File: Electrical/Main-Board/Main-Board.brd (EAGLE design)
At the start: 160 x 100 mm, 0 parts

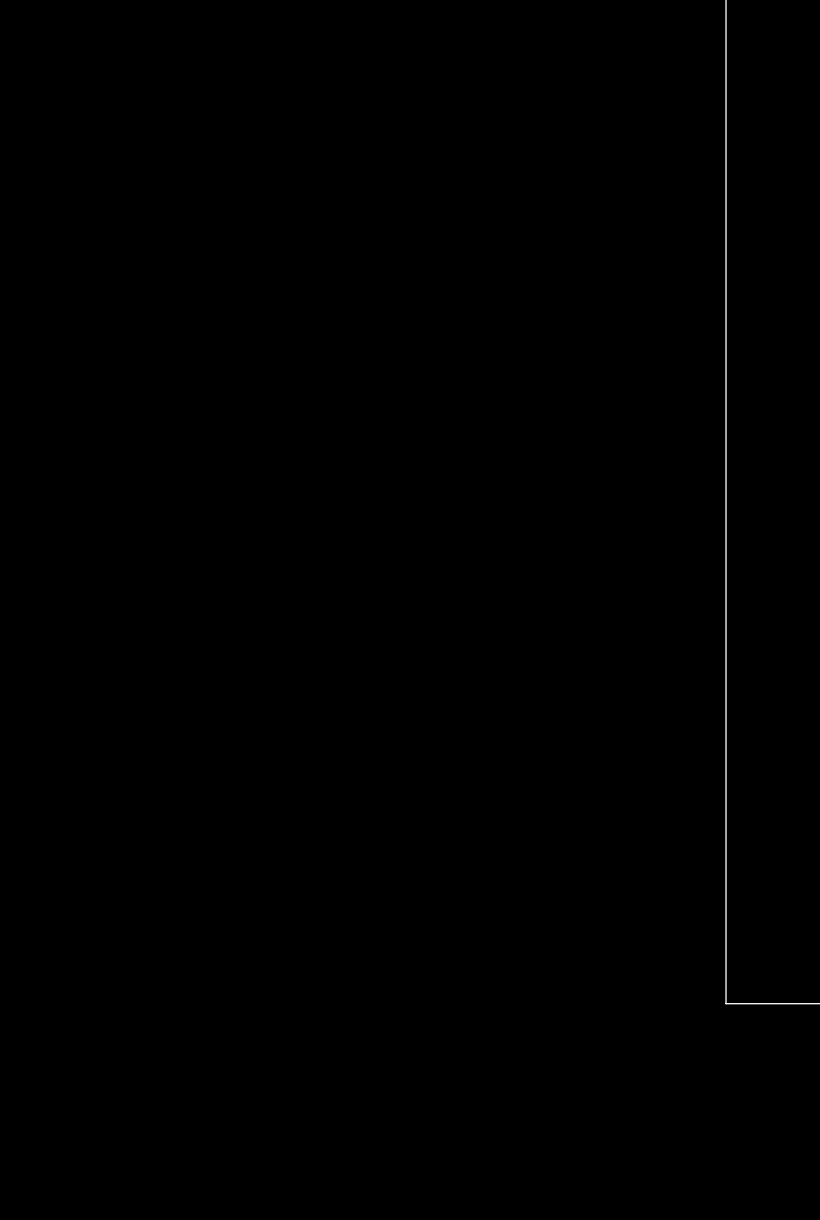
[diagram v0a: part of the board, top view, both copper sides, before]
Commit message: Updated schematic and ignore all backup files
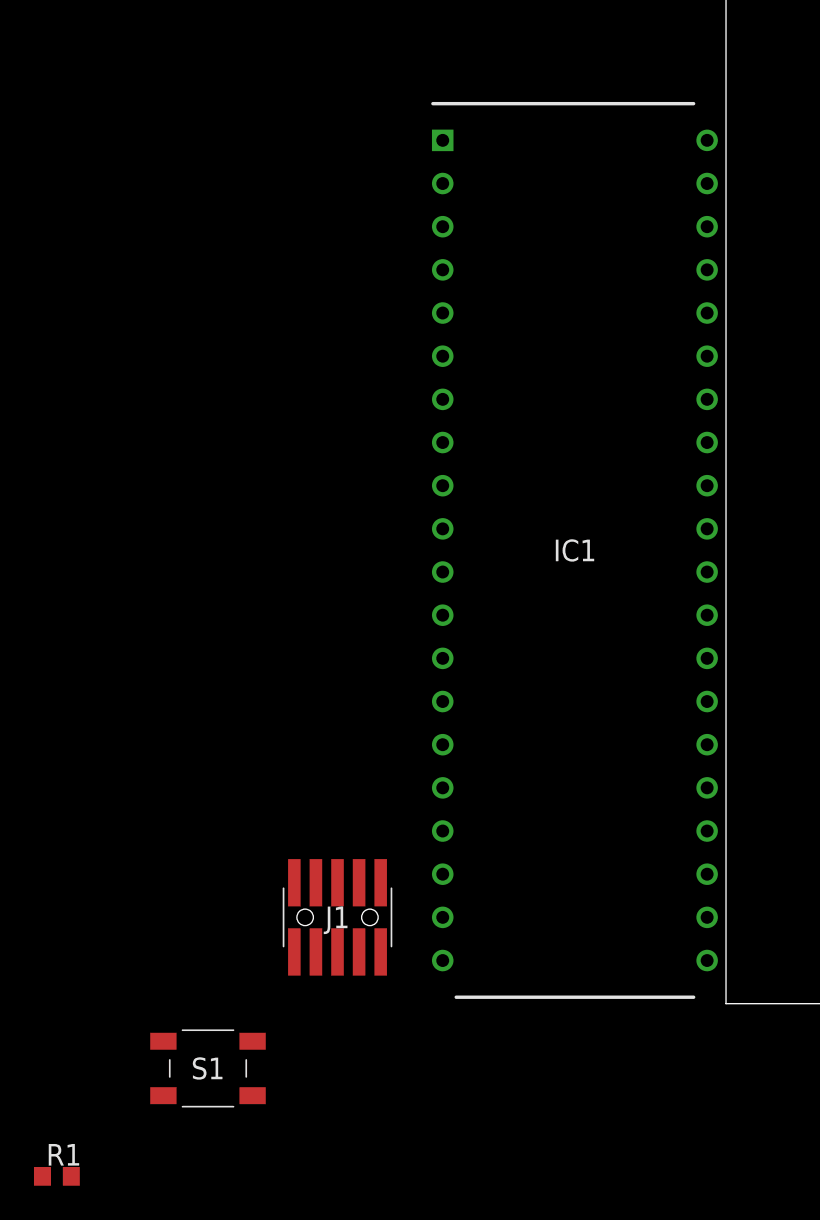
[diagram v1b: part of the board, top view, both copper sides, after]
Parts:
- added IC1: ATMEGA16A-PU, SamacSys_Parts:DIP1556W56P254L5232H483Q40N
- added J1: FTSH-105-01-L-DV-K-A-P-TR, SamacSys_Parts:FTSH10501LDVKAPTR
- added R1: 10K/10%, rcl:R0603
- added S1: PTS647SM50SMTR2LFS, SamacSys_Parts:PTS647SM50SMTR2LFS
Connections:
- new net +5V/1: IC1.10, IC1.30, IC1.32, J1.7, R1.2
- new net GND: IC1.11, IC1.31, J1.10, J1.6, S1.3, S1.4
- new net RST: IC1.9, J1.8, R1.1, S1.1, S1.2
- new net TCK: IC1.24, J1.1
- new net TDI: IC1.27, J1.5
- new net TDO: IC1.26, J1.2
- new net TMS: IC1.25, J1.3
- new net TRST: J1.9
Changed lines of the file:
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@@
 <drawing>
 <settings>
-<setting alwaysvectorfont="yes"/>
+<setting alwaysvectorfont="no"/>
 <setting verticaltext="up"/>
 </settings>
@@
 </autorouter>
 <elements>
+<element name="IC1" library="SamacSys_Parts" package="DIP1556W56P254L5232H483Q40N" value="ATMEGA16A-PU" x="-8.89" y="26.67" smashed="yes">
+<attribute name="DESCRIPTION" value="ATMEGA16A-PU, 8 bit AVR Microcontroller 16MHz 16 kB, 512 B Flash, 1 kB RAM, I2C 40-Pin PDIP" x="-8.89" y="26.67" size="1.778" layer="27" display="off"/>
+<attribute name="HEIGHT" value="4.826mm" x="-8.89" y="26.67" size="1.778" layer="27" display="off"/>
+<attribute name="MANUFACTURER_NAME" value="Microchip" x="-8.89" y="26.67" size="1.778" layer="27" display="off"/>
+<attribute name="MANUFACTURER_PART_NUMBER" value="ATMEGA16A-PU" x="-8.89" y="26.67" size="1.778" layer="27" display="off"/>
+<attribute name="MOUSER_PART_NUMBER" value="556-ATMEGA16A-PU" x="-8.89" y="26.67" size="1.778" layer="27" display="off"/>
+<attribute name="MOUSER_PRICE-STOCK" value="https://www.mouser.com/Search/Refine.aspx?Keyword=556-ATMEGA16A-PU" x="-8.89" y="26.67" size="1.778" layer="27" display="off"/>
+<attribute name="NAME" x="-8.89" y="26.67" size="1.27" layer="25" align="center"/>
+<attribute name="RS_PART_NUMBER" value="6962421P" x="-8.89" y="26.67" size="1.778" layer="27" display="off"/>
+<attribute name="RS_PRICE-STOCK" value="http://uk.rs-online.com/web/p/products/6962421P" x="-8.89" y="26.67" size="1.778" layer="27" display="off"/>
+<attribute name="VALUE" x="-8.89" y="26.67" size="1.27" layer="27" align="center"/>
+</element>
+<element name="J1" library="SamacSys_Parts" package="FTSH10501LDVKAPTR" value="FTSH-105-01-L-DV-K-A-P-TR" x="-22.86" y="5.08" smashed="yes">
+<attribute name="DESCRIPTION" value="Samtec FTSH, 1.27mm Pitch, 10 Way, 2 Row PCB Terminal Block Header, Surface Mount, Through Hole" x="-22.86" y="5.08" size="1.778" layer="27" display="off"/>
+<attribute name="HEIGHT" value="6.1mm" x="-22.86" y="5.08" size="1.778" layer="27" display="off"/>
+<attribute name="MANUFACTURER_NAME" value="SAMTEC" x="-22.86" y="5.08" size="1.778" layer="27" display="off"/>
+<attribute name="MANUFACTURER_PART_NUMBER" value="FTSH-105-01-L-DV-K-A-P-TR" x="-22.86" y="5.08" size="1.778" layer="27" display="off"/>
+<attribute name="MOUSER_PART_NUMBER" value="200-FTSH1051LDVKAPTR" x="-22.86" y="5.08" size="1.778" layer="27" display="off"/>
+<attribute name="MOUSER_PRICE-STOCK" value="https://www.mouser.com/Search/Refine.aspx?Keyword=200-FTSH1051LDVKAPTR" x="-22.86" y="5.08" size="1.778" layer="27" display="off"/>
+<attribute name="NAME" x="-22.86" y="5.08" size="1.27" layer="25" align="center"/>
+<attribute name="RS_PART_NUMBER" value="1802978P" x="-22.86" y="5.08" size="1.778" layer="27" display="off"/>
+<attribute name="RS_PRICE-STOCK" value="http://uk.rs-online.com/web/p/products/1802978P" x="-22.86" y="5.08" size="1.778" layer="27" display="off"/>
+<attribute name="VALUE" x="-22.86" y="5.08" size="1.27" layer="27" align="center"/>
+</element>
+<element name="S1" library="SamacSys_Parts" package="PTS647SM50SMTR2LFS" value="PTS647SM50SMTR2LFS" x="-30.48" y="-3.81" smashed="yes">
+<attribute name="DESCRIPTION" value="Tactile Switches 50mA 12VDC, 1.8N 5.0mm H, G leads" x="-30.48" y="-3.81" size="1.778" layer="27" display="off"/>
+<attribute name="HEIGHT" value="5.25mm" x="-30.48" y="-3.81" size="1.778" layer="27" display="off"/>
+<attribute name="MANUFACTURER_NAME" value="C &amp; K COMPONENTS" x="-30.48" y="-3.81" size="1.778" layer="27" display="off"/>
+<attribute name="MANUFACTURER_PART_NUMBER" value="PTS647SM50SMTR2LFS" x="-30.48" y="-3.81" size="1.778" layer="27" display="off"/>
+<attribute name="MOUSER_PART_NUMBER" value="611-PTS647SM50SMTR2L" x="-30.48" y="-3.81" size="1.778" layer="27" display="off"/>
+<attribute name="MOUSER_PRICE-STOCK" value="https://www.mouser.com/Search/Refine.aspx?Keyword=611-PTS647SM50SMTR2L" x="-30.48" y="-3.81" size="1.778" layer="27" display="off"/>
+<attribute name="NAME" x="-30.48" y="-3.81" size="1.27" layer="25" align="center"/>
+<attribute name="RS_PART_NUMBER" value="" x="-30.48" y="-3.81" size="1.778" layer="27" display="off"/>
+<attribute name="RS_PRICE-STOCK" value="" x="-30.48" y="-3.81" size="1.778" layer="27" display="off"/>
+<attribute name="VALUE" x="-30.48" y="-3.81" size="1.27" layer="27" align="center"/>
+</element>
+<element name="R1" library="rcl" library_urn="urn:adsk.eagle:library:334" package="R0603" package3d_urn="urn:adsk.eagle:package:23555/3" value="10K/10%" x="-39.37" y="-10.16" smashed="yes">
+<attribute name="NAME" x="-40.005" y="-9.525" size="1.27" layer="25"/>
+<attribute name="POPULARITY" value="70" x="-39.37" y="-10.16" size="1.778" layer="27" display="off"/>
+<attribute name="SPICEPREFIX" value="R" x="-39.37" y="-10.16" size="1.778" layer="27" display="off"/>
+<attribute name="VALUE" x="-40.005" y="-12.065" size="1.27" layer="27"/>
+</element>
 </elements>
 <signals>
+<signal name="GND">
+<contactref element="IC1" pad="11"/>
+<contactref element="IC1" pad="31"/>
+<contactref element="J1" pad="6"/>
+<contactref element="J1" pad="10"/>
+<contactref element="S1" pad="4"/>
+<contactref element="S1" pad="3"/>
+<wire x1="-27.855" y1="-2.21" x2="-27.855" y2="-5.41" width="0" layer="19" extent="1-1"/>
+<wire x1="-22.86" y1="7.115" x2="-27.855" y2="-2.21" width="0" layer="19" extent="1-1"/>
+<wire x1="-20.32" y1="7.115" x2="-22.86" y2="7.115" width="0" layer="19" extent="1-1"/>
+<wire x1="-16.669" y1="25.4" x2="-20.32" y2="7.115" width="0" layer="19" extent="1-1"/>
+<wire x1="-1.111" y1="27.94" x2="-16.669" y2="25.4" width="0" layer="19" extent="1-1"/>
+</signal>
+<signal name="+5V/1">
+<contactref element="IC1" pad="30"/>
+<contactref element="IC1" pad="32"/>
+<contactref element="IC1" pad="10"/>
+<contactref element="J1" pad="7"/>
+<contactref element="R1" pad="2"/>
+<wire x1="-21.59" y1="3.045" x2="-38.52" y2="-10.16" width="0" layer="19" extent="1-1"/>
+<wire x1="-16.669" y1="27.94" x2="-21.59" y2="3.045" width="0" layer="19" extent="1-1"/>
+<wire x1="-1.111" y1="30.48" x2="-16.669" y2="27.94" width="0" layer="19" extent="1-1"/>
+<wire x1="-1.111" y1="25.4" x2="-1.111" y2="30.48" width="0" layer="19" extent="1-1"/>
+</signal>
+<signal name="TCK">
+<contactref element="J1" pad="1"/>
+<contactref element="IC1" pad="24"/>
+<wire x1="-1.111" y1="10.16" x2="-25.4" y2="3.045" width="0" layer="19" extent="1-1"/>
+</signal>
+<signal name="RST">
+<contactref element="J1" pad="8"/>
+<contactref element="S1" pad="1"/>
+<contactref element="S1" pad="2"/>
+<contactref element="IC1" pad="9"/>
+<contactref element="R1" pad="1"/>
+<wire x1="-33.105" y1="-5.41" x2="-40.22" y2="-10.16" width="0" layer="19" extent="1-1"/>
+<wire x1="-33.105" y1="-2.21" x2="-33.105" y2="-5.41" width="0" layer="19" extent="1-1"/>
+<wire x1="-21.59" y1="7.115" x2="-33.105" y2="-2.21" width="0" layer="19" extent="1-1"/>
+<wire x1="-16.669" y1="30.48" x2="-21.59" y2="7.115" width="0" layer="19" extent="1-1"/>
+</signal>
+<signal name="TRST">
+<contactref element="J1" pad="9"/>
+</signal>
+<signal name="TDO">
+<contactref element="J1" pad="2"/>
+<contactref element="IC1" pad="26"/>
+<wire x1="-1.111" y1="15.24" x2="-25.4" y2="7.115" width="0" layer="19" extent="1-1"/>
+</signal>
+<signal name="TMS">
+<contactref element="J1" pad="3"/>
+<contactref element="IC1" pad="25"/>
+<wire x1="-1.111" y1="12.7" x2="-24.13" y2="3.045" width="0" layer="19" extent="1-1"/>
+</signal>
+<signal name="TDI">
+<contactref element="J1" pad="5"/>
+<contactref element="IC1" pad="27"/>
+<wire x1="-1.111" y1="17.78" x2="-22.86" y2="3.045" width="0" layer="19" extent="1-1"/>
+</signal>
 </signals>
 <mfgpreviewcolors>
@@
 </board>
 </drawing>
+<compatibility>
+<note version="8.2" severity="warning">
+Since Version 8.2, EAGLE supports online libraries. The ids
+of those online libraries will not be understood (or retained)
+with this version.
+</note>
+<note version="8.3" severity="warning">
+Since Version 8.3, EAGLE supports URNs for individual library
+assets (packages, symbols, and devices). The URNs of those assets
+will not be understood (or retained) with this version.
+</note>
+<note version="8.3" severity="warning">
+Since Version 8.3, EAGLE supports the association of 3D packages
+with devices in libraries, schematics, and board files. Those 3D
+packages will not be understood (or retained) with this version.
+</note>
+</compatibility>
 </eagle>

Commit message: Updated schematic
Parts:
- added R2, R3: 10K/10%, rcl:R0603
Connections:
- new net LCD-DB0: IC1.40
- new net LCD-DB1: IC1.39
- new net LCD-DB2: IC1.38
- new net LCD-DB3: IC1.37
- new net LCD-DB4: IC1.36
- new net LCD-DB5: IC1.35
- new net LCD-DB6: IC1.34
- new net LCD-DB7: IC1.33
- new net SCL: IC1.22, R3.1
- new net SDA: IC1.23, R2.1
- net +5V/1: now also R2.2, R3.2
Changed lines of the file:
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@@
 <attribute name="VALUE" x="-40.005" y="-12.065" size="1.27" layer="27"/>
+</element>
+<element name="R2" library="rcl" library_urn="urn:adsk.eagle:library:334" package="R0603" package3d_urn="urn:adsk.eagle:package:23555/3" value="10K/10%" x="-39.37" y="-15.24" smashed="yes">
+<attribute name="NAME" x="-40.005" y="-14.605" size="1.27" layer="25"/>
+<attribute name="POPULARITY" value="70" x="-39.37" y="-15.24" size="1.778" layer="27" display="off"/>
+<attribute name="SPICEPREFIX" value="R" x="-39.37" y="-15.24" size="1.778" layer="27" display="off"/>
+<attribute name="VALUE" x="-40.005" y="-17.145" size="1.27" layer="27"/>
+</element>
+<element name="R3" library="rcl" library_urn="urn:adsk.eagle:library:334" package="R0603" package3d_urn="urn:adsk.eagle:package:23555/3" value="10K/10%" x="-39.37" y="-20.32" smashed="yes">
+<attribute name="NAME" x="-40.005" y="-19.685" size="1.27" layer="25"/>
+<attribute name="POPULARITY" value="70" x="-39.37" y="-20.32" size="1.778" layer="27" display="off"/>
+<attribute name="SPICEPREFIX" value="R" x="-39.37" y="-20.32" size="1.778" layer="27" display="off"/>
+<attribute name="VALUE" x="-40.005" y="-22.225" size="1.27" layer="27"/>
 </element>
 </elements>
@@
 <contactref element="J1" pad="7"/>
 <contactref element="R1" pad="2"/>
+<contactref element="R2" pad="2"/>
+<contactref element="R3" pad="2"/>
+<wire x1="-38.52" y1="-15.24" x2="-38.52" y2="-20.32" width="0" layer="19" extent="1-1"/>
+<wire x1="-38.52" y1="-10.16" x2="-38.52" y2="-15.24" width="0" layer="19" extent="1-1"/>
 <wire x1="-21.59" y1="3.045" x2="-38.52" y2="-10.16" width="0" layer="19" extent="1-1"/>
 <wire x1="-16.669" y1="27.94" x2="-21.59" y2="3.045" width="0" layer="19" extent="1-1"/>
@@
 <wire x1="-1.111" y1="17.78" x2="-22.86" y2="3.045" width="0" layer="19" extent="1-1"/>
 </signal>
+<signal name="SDA">
+<contactref element="IC1" pad="23"/>
+<contactref element="R2" pad="1"/>
+<wire x1="-1.111" y1="7.62" x2="-40.22" y2="-15.24" width="0" layer="19" extent="1-1"/>
+</signal>
+<signal name="SCL">
+<contactref element="IC1" pad="22"/>
+<contactref element="R3" pad="1"/>
+<wire x1="-1.111" y1="5.08" x2="-40.22" y2="-20.32" width="0" layer="19" extent="1-1"/>
+</signal>
+<signal name="LCD-DB0">
+<contactref element="IC1" pad="40"/>
+</signal>
+<signal name="LCD-DB1">
+<contactref element="IC1" pad="39"/>
+</signal>
+<signal name="LCD-DB2">
+<contactref element="IC1" pad="38"/>
+</signal>
+<signal name="LCD-DB3">
+<contactref element="IC1" pad="37"/>
+</signal>
+<signal name="LCD-DB4">
+<contactref element="IC1" pad="36"/>
+</signal>
+<signal name="LCD-DB5">
+<contactref element="IC1" pad="35"/>
+</signal>
+<signal name="LCD-DB6">
+<contactref element="IC1" pad="34"/>
+</signal>
+<signal name="LCD-DB7">
+<contactref element="IC1" pad="33"/>
+</signal>
 </signals>

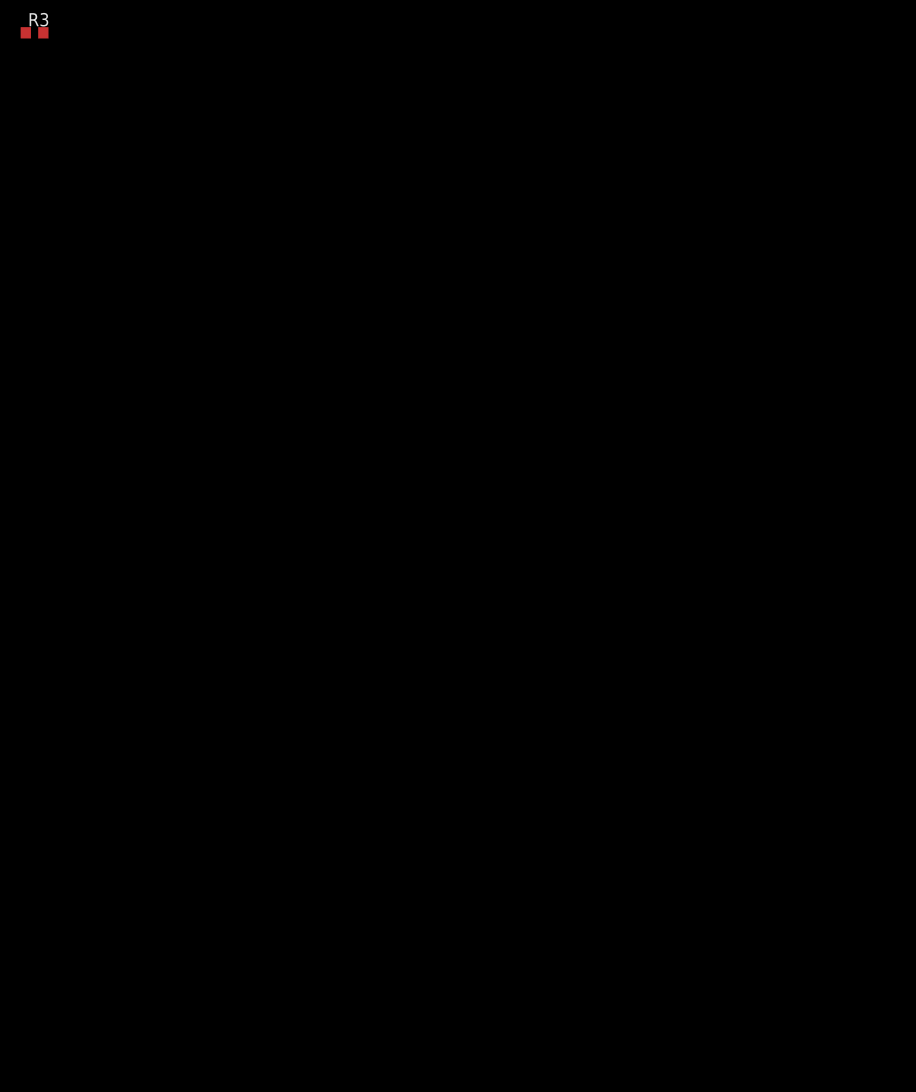
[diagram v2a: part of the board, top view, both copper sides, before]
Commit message: Updated schematic
Added a similar LCD and µC:2
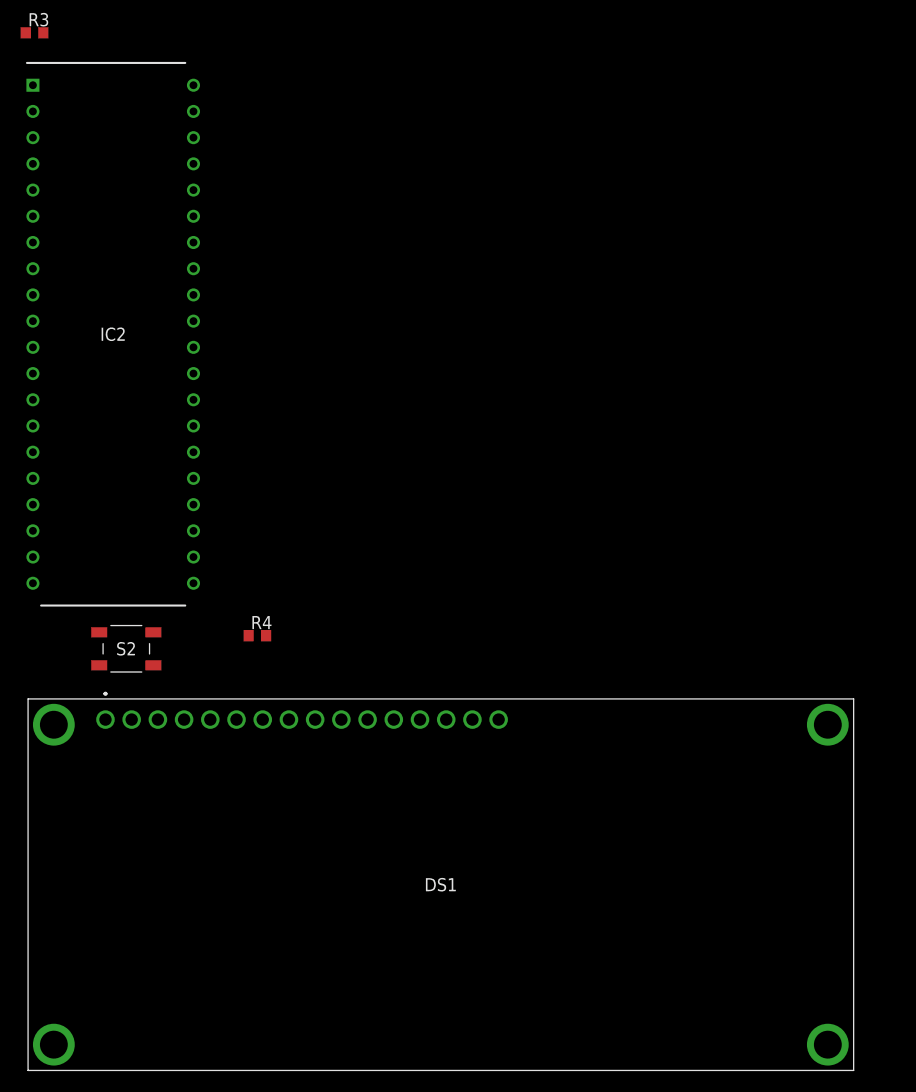
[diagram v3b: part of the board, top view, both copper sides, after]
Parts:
- added DS1: NHD-0216XZ-FSW-GBW, SamacSys_Parts:NHD0216XZFSWGBW
- added IC2: ATMEGA16A-PU, SamacSys_Parts:DIP1556W56P254L5232H483Q40N
- added R4: 10K/10%, rcl:R0603
- added S2: PTS647SM50SMTR2LFS, SamacSys_Parts:PTS647SM50SMTR2LFS
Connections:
- new net LCD-E: DS1.6, IC1.18
- new net LCD-R/W: DS1.5, IC1.19
- new net LCD-RS: DS1.4, IC1.20
- new net LOWER-DISK-LIMIT: IC2.17
- new net N$2: DS1.3
- new net UPPER-DISK-LIMIT: IC2.16
- net +5V/1: now also DS1.2, IC2.10, IC2.30, IC2.32, R4.2
- net GND: now also DS1.1, IC2.11, IC2.31, S2.3, S2.4
- net LCD-DB0: now also DS1.7
- net LCD-DB1: now also DS1.8
- net LCD-DB2: now also DS1.9
- net LCD-DB3: now also DS1.10
- net LCD-DB4: now also DS1.11
- net LCD-DB5: now also DS1.12
- net LCD-DB6: now also DS1.13
- net LCD-DB7: now also DS1.14
- net RST: now also IC2.9, R4.1, S2.1, S2.2
- net SCL: now also IC2.22
- net SDA: now also IC2.23
- net TCK: now also IC2.24
- net TDI: now also IC2.27
- net TDO: now also IC2.26
- net TMS: now also IC2.25
